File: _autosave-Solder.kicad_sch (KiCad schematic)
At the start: 5 parts

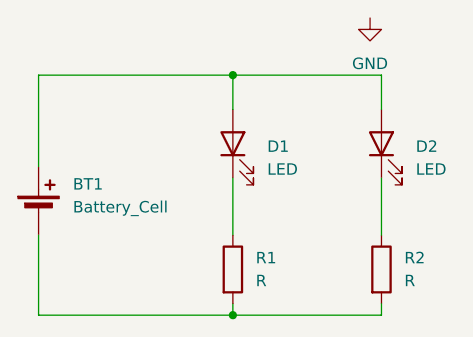
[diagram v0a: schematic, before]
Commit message: add ground pour
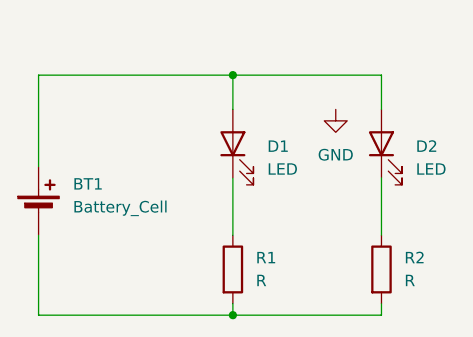
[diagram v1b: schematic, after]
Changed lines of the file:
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@@
 	(symbol
 		(lib_id "power:GND")
-		(at 142.24 57.15 0)
+		(at 138.43 67.31 0)
 		(unit 1)
 		(exclude_from_sim no)
@@
 		(fields_autoplaced yes)
 		(property "Reference" "#PWR01"
-			(at 142.24 63.5 0)
+			(at 138.43 73.66 0)
 			(effects
 				(font
@@
 		)
 		(property "Value" "GND"
-			(at 142.24 62.23 0)
+			(at 138.43 72.39 0)
 			(effects
 				(font
@@
 		)
 		(property "Footprint" ""
-			(at 142.24 57.15 0)
+			(at 138.43 67.31 0)
 			(effects
 				(font
@@
 		)
 		(property "Datasheet" ""
-			(at 142.24 57.15 0)
+			(at 138.43 67.31 0)
 			(effects
 				(font
@@
 		)
 		(property "Description" "Power symbol creates a global label with name \"GND\" , ground"
-			(at 142.24 57.15 0)
+			(at 138.43 67.31 0)
 			(effects
 				(font
